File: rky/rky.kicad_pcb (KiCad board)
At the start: 2 copper layers, 24.9 x 41.1 mm, 59 parts, among them J1 Conn_01x02_Male, J2 Li-Ion 3.7 CONN, J3 USB_C_Receptacle_USB2.0, J4 Conn_01x04_Male, J5 Conn_02x03_Odd_Even, U2 SSD1306, U3 ESP8266-12E/ESP-12E, U4 LM3940IMP-3.3/NOPB, U5 TP4056, U6 NRF24L01, Y1 16MHZ

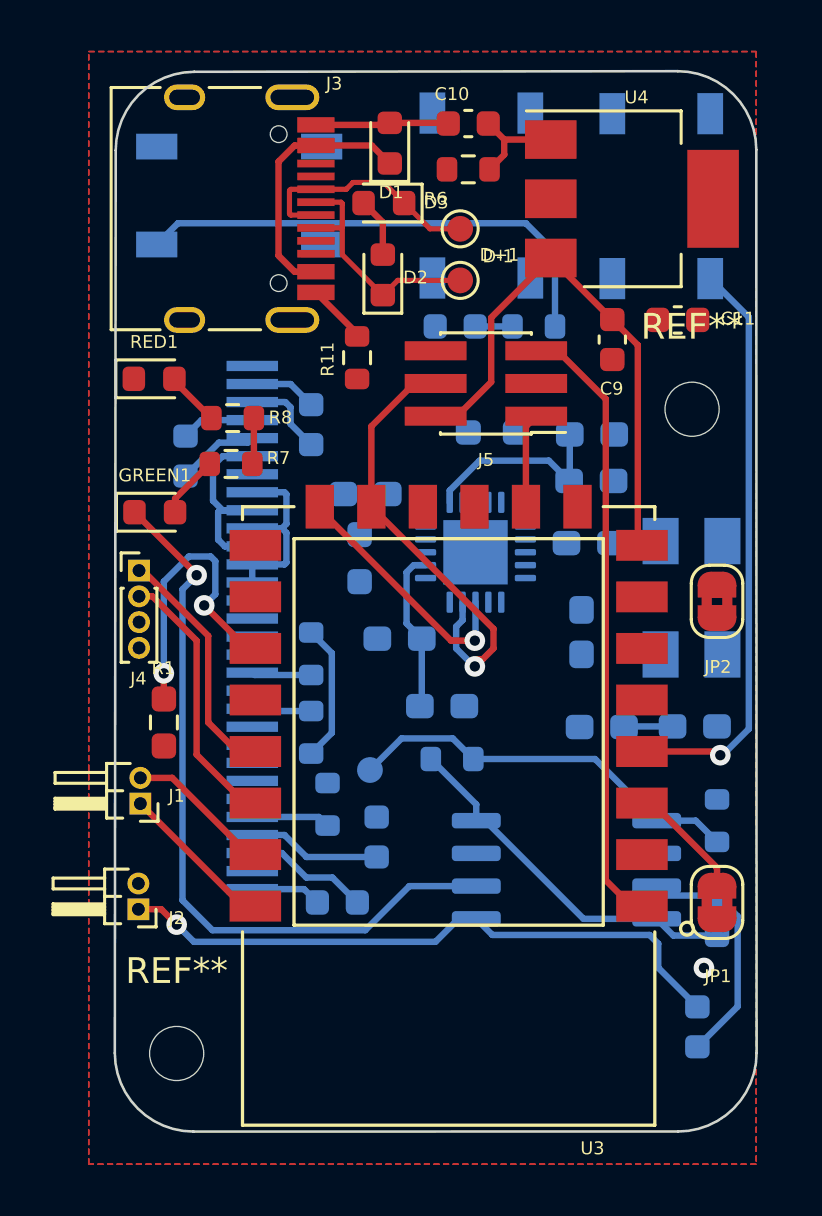
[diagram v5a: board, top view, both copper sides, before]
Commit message: update README
 add render images
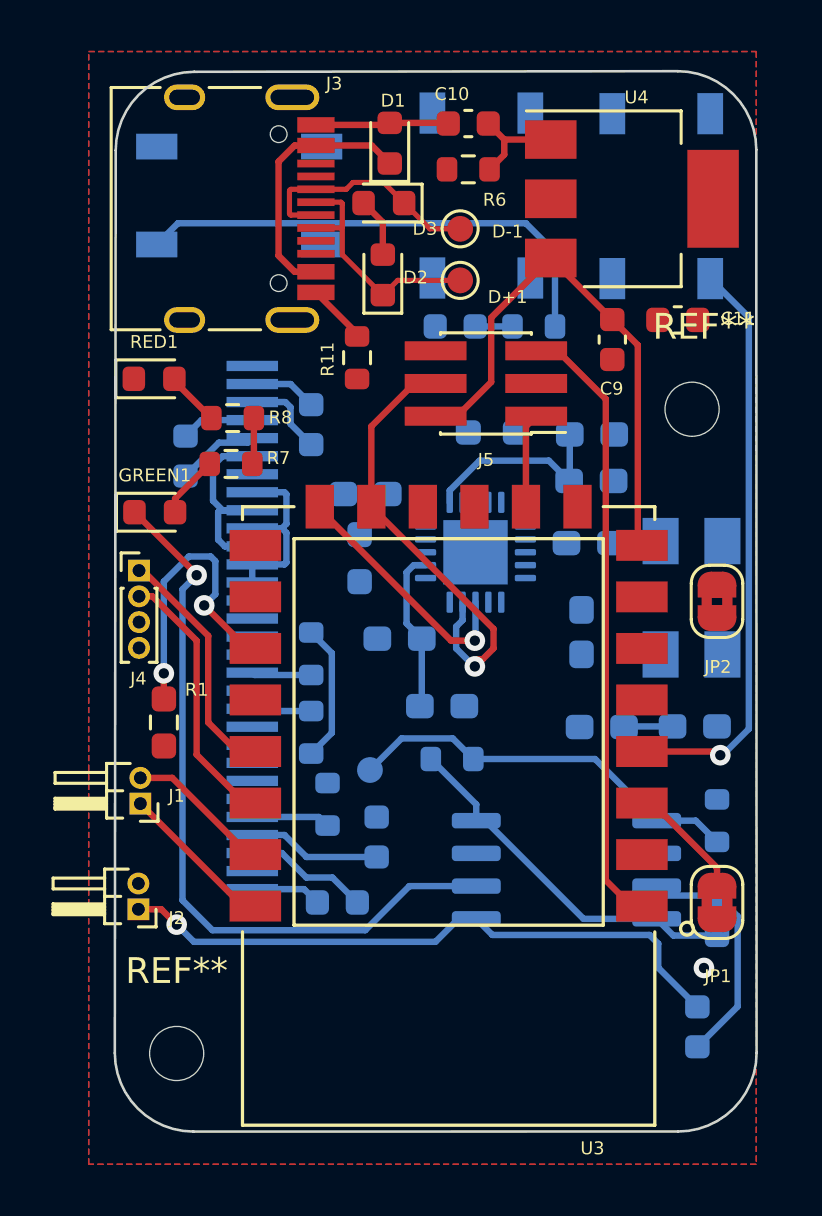
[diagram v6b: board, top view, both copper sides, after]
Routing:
- removed copper zone on F.Cu, net VCC
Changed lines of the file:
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@@
     (property "Sheetname" "")
     (attr exclude_from_pos_files)
-    (fp_text reference "D+1" (at 1.524 -0.9906) (layer "F.SilkS")
+    (fp_text reference "D+1" (at 1.84 0.645) (layer "F.SilkS")
       (effects (font (size 0.5 0.5) (thickness 1.5)))
     )
@@
     (tags "mounting hole 2.1mm no annular")
     (attr exclude_from_pos_files exclude_from_bom)
-    (fp_text reference "REF**" (at 0 -3.2) (layer "F.SilkS")
+    (fp_text reference "REF**" (at 0.46 -3.2) (layer "F.SilkS")
       (effects (font (size 1 1) (thickness 0.15)))
     )
@@
     (property "Sheetname" "")
     (attr smd)
-    (fp_text reference "R6" (at -1.27 1.143) (layer "F.SilkS")
+    (fp_text reference "R6" (at 1.022518 1.179407) (layer "F.SilkS")
       (effects (font (size 0.5 0.5) (thickness 1.5)))
     )
@@
     (property "Sheetname" "")
     (attr smd)
-    (fp_text reference "D1" (at -1.905 0.0508) (layer "F.SilkS")
+    (fp_text reference "D1" (at 1.651 0.127) (layer "F.SilkS")
       (effects (font (size 0.5 0.5) (thickness 1.5)))
     )
@@
     (property "Sheetname" "")
     (attr exclude_from_pos_files)
-    (fp_text reference "D-1" (at 1.4732 1.0668) (layer "F.SilkS")
+    (fp_text reference "D-1" (at 1.84 0.105) (layer "F.SilkS")
       (effects (font (size 0.5 0.5) (thickness 1.5)))
     )
@@
     (property "Sheetname" "")
     (attr smd)
-    (fp_text reference "D3" (at -2.0319 0.0254) (layer "F.SilkS")
+    (fp_text reference "D3" (at -1.592493 -1) (layer "F.SilkS")
       (effects (font (size 0.5 0.5) (thickness 1.5)))
     )
@@
     (property "Sheetname" "")
     (attr smd)
-    (fp_text reference "R1" (at 2.1082 -0.0254 180) (layer "F.SilkS")
+    (fp_text reference "R1" (at 1.27 1.27 180) (layer "F.SilkS")
       (effects (font (size 0.5 0.5) (thickness 1.5)))
     )
@@
     (property "Sheetname" "")
     (attr smd)
-    (fp_text reference "C7" (at 0 1.43 90) (layer "B.SilkS")
+    (fp_text reference "C7" (at 0 1.27 180) (layer "B.SilkS")
       (effects (font (size 0.5 0.5) (thickness 1.5)) (justify mirror))
     )
@@
     (property "Sheetname" "")
     (attr smd)
-    (fp_text reference "C12" (at 0 1.43 90) (layer "B.SilkS")
+    (fp_text reference "C12" (at 1.953551 -0.321227 180) (layer "B.SilkS")
       (effects (font (size 0.5 0.5) (thickness 1.5)) (justify mirror))
     )
@@
     (property "Sheetname" "")
     (attr smd)
-    (fp_text reference "U2" (at -0.35 -2.1 90) (layer "B.SilkS")
+    (fp_text reference "U2" (at -1.397 -2.1 180) (layer "B.SilkS")
       (effects (font (size 0.5 0.5) (thickness 1.5)) (justify mirror))
     )
@@
     (pad "30" smd rect (at 10.15 0 270) (size 0.4 2) (layers "B.Cu" "B.Paste" "B.Mask")
       (net 3 "GND") (pinfunction "NC") (pintype "input"))
-    (model "${KICAD6_3DMODEL_DIR}/Display.3dshapes/OLED-128O064D.wrl" hide
+    (model "${KICAD6_3DMODEL_DIR}/Display.3dshapes/OLED-128O064D.wrl"
       (offset (xyz 0 -6 3.2))
       (scale (xyz 1 1 1))
@@
     (property "Sheetname" "")
     (attr smd)
-    (fp_text reference "R3" (at 0 1.43 90) (layer "B.SilkS")
+    (fp_text reference "R3" (at 0.908291 1.095527 180) (layer "B.SilkS")
       (effects (font (size 0.5 0.5) (thickness 1.5)) (justify mirror))
     )
@@
     (property "Sheetname" "")
     (attr smd)
-    (fp_text reference "U6" (at 0 3.3 90) (layer "B.SilkS")
+    (fp_text reference "U6" (at -2.992645 -0.92781 180) (layer "B.SilkS")
       (effects (font (size 0.5 0.5) (thickness 1.5)) (justify mirror))
     )
@@
     (property "Sheetname" "")
     (attr smd)
-    (fp_text reference "C16" (at 0 1.43) (layer "B.SilkS")
+    (fp_text reference "C16" (at 0.212504 -1.282902) (layer "B.SilkS")
       (effects (font (size 0.5 0.5) (thickness 1.5)) (justify mirror))
     )
@@
     (property "Sheetname" "")
     (attr smd)
-    (fp_text reference "C19" (at 0 1.43) (layer "B.SilkS")
+    (fp_text reference "C19" (at -0.522873 -1.147819) (layer "B.SilkS")
       (effects (font (size 0.5 0.5) (thickness 1.5)) (justify mirror))
     )
@@
     (property "Sheetname" "")
     (attr smd)
-    (fp_text reference "C15" (at 0 1.43) (layer "B.SilkS")
+    (fp_text reference "C15" (at 0.444194 1.10826) (layer "B.SilkS")
       (effects (font (size 0.5 0.5) (thickness 1.5)) (justify mirror))
     )
@@
     (property "Sheetname" "")
     (attr smd)
-    (fp_text reference "C8" (at 0 1.43) (layer "B.SilkS")
+    (fp_text reference "C8" (at -2.051356 -1.085948) (layer "B.SilkS")
       (effects (font (size 0.5 0.5) (thickness 1.5)) (justify mirror))
     )
@@
     (property "Sheetname" "")
     (attr smd)
-    (fp_text reference "R2" (at 0 1.43 -270) (layer "B.SilkS")
+    (fp_text reference "R2" (at 0 -1.27 -180) (layer "B.SilkS")
       (effects (font (size 0.5 0.5) (thickness 1.5)) (justify mirror))
     )
@@
     (property "Sheetname" "")
     (attr smd)
-    (fp_text reference "C2" (at 0 1.43) (layer "B.SilkS")
+    (fp_text reference "C2" (at 0 -1.27) (layer "B.SilkS")
       (effects (font (size 0.5 0.5) (thickness 1.5)) (justify mirror))
     )
@@
     (property "Sheetname" "")
     (attr smd)
-    (fp_text reference "R10" (at 0 1.43 90) (layer "B.SilkS")
+    (fp_text reference "R10" (at -1.144361 1.498192 180) (layer "B.SilkS")
       (effects (font (size 0.5 0.5) (thickness 1.5)) (justify mirror))
     )
@@
     (property "Sheetname" "")
     (attr smd)
-    (fp_text reference "C4" (at 0 1.43) (layer "B.SilkS")
+    (fp_text reference "C4" (at -1.208265 1.062454) (layer "B.SilkS")
       (effects (font (size 0.5 0.5) (thickness 1.5)) (justify mirror))
     )
@@
     (property "Sheetname" "")
     (attr through_hole)
-    (fp_text reference "SELECT1" (at -0.00001 3.68852 90) (layer "B.SilkS")
+    (fp_text reference "SELECT1" (at -0.02362 10.409815 90) (layer "B.SilkS")
       (effects (font (size 0.5 0.5) (thickness 1.5)) (justify mirror))
     )
@@
     (property "Sheetname" "")
     (attr smd)
-    (fp_text reference "R13" (at 0 1.43 90) (layer "B.SilkS")
+    (fp_text reference "R13" (at 0 1.43 180) (layer "B.SilkS")
       (effects (font (size 0.5 0.5) (thickness 1.5)) (justify mirror))
     )
@@
     (property "Sheetname" "")
     (attr smd)
-    (fp_text reference "R5" (at 0 1.43 90) (layer "B.SilkS")
+    (fp_text reference "R5" (at -2.007889 -0.675747 180) (layer "B.SilkS")
       (effects (font (size 0.5 0.5) (thickness 1.5)) (justify mirror))
     )
@@
     (property "Sheetname" "")
     (attr exclude_from_pos_files)
-    (fp_text reference "B_TEMP1" (at 0 1.448) (layer "B.SilkS")
+    (fp_text reference "B_TEMP1" (at -0.970111 1.432525) (layer "B.SilkS")
       (effects (font (size 0.5 0.5) (thickness 1.5)) (justify mirror))
     )
@@
     (property "Sheetname" "")
     (attr smd)
-    (fp_text reference "C5" (at 0 1.43 90) (layer "B.SilkS")
+    (fp_text reference "C5" (at 0 1.43 180) (layer "B.SilkS")
       (effects (font (size 0.5 0.5) (thickness 1.5)) (justify mirror))
     )
@@
     (property "Sheetname" "")
     (attr smd)
-    (fp_text reference "C13" (at 0 1.43 90) (layer "B.SilkS")
+    (fp_text reference "C13" (at -1.691402 0.702234 180) (layer "B.SilkS")
       (effects (font (size 0.5 0.5) (thickness 1.5)) (justify mirror))
     )
@@
     (connect_pads (clearance 0.508))
     (min_thickness 0.254) (filled_areas_thickness no)
-    (fill yes (thermal_gap 0.508) (thermal_bridge_width 0.508))
-    (polygon
-      (pts
-        (xy 126.492 114.3)
-        (xy 100.584 114.3)
-        (xy 100.584 71.12)
-        (xy 126.492 71.12)
-      )
-    )
-  )
-  (zone (net 14) (net_name "VCC") (layer "F.Cu") (hatch edge 0.508)
-    (connect_pads (clearance 0.508))
-    (min_thickness 0.254) (filled_areas_thickness no)
